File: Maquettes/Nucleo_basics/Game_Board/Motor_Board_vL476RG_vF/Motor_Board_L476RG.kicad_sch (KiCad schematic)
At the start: 41 parts, among them CON1 MikroE-Accelero, CON2 MikroE-nRF-S-module, J1 Speed_R, J10 Morpho_Gauche, J11 Morpho_Droite, J12 LED_1, J13 LED_2, J14 LED_3, J15 LED_4, J17 I2C_Visu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

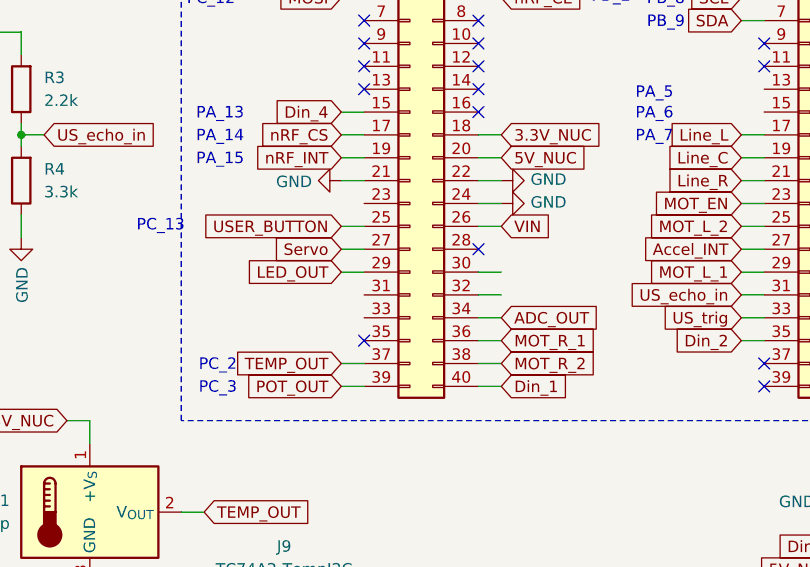
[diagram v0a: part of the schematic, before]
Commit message: Update Nucleo Basics / Remote and Robot Boards
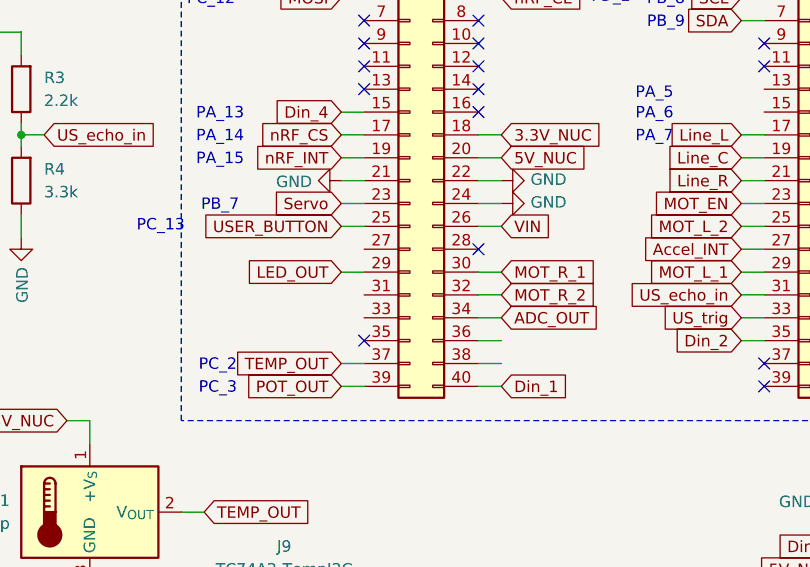
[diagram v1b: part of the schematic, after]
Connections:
- net MOT_R_1: now also J10.30 (Pin_30); no longer J10.36 (Pin_36)
- net MOT_R_2: now also J10.32 (Pin_32); no longer J10.38 (Pin_38)
- net Servo: now also J10.23 (Pin_23); no longer J10.27 (Pin_27)
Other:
- note added: "PB_7"
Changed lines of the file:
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@@
+	(wire
+		(pts
+			(xy 96.52 81.28) (xy 99.06 81.28)
+		)
+		(stroke
+			(width 0)
+			(type default)
+		)
+	)
 	(wire
 		(pts
@@
 	(wire
 		(pts
-			(xy 96.52 86.36) (xy 99.06 86.36)
-		)
-		(stroke
-			(width 0)
-			(type default)
-		)
-	)
-	(wire
-		(pts
 			(xy 199.39 154.94) (xy 196.85 154.94)
 		)
@@
 		)
 	)
+	(text "PB_7"
+		(exclude_from_sim no)
+		(at 83.058 81.534 0)
+		(effects
+			(font
+				(size 1.27 1.27)
+			)
+		)
+	)
 	(text "Nucleo BOARD"
 		(exclude_from_sim no)
@@
 	(global_label "Servo"
 		(shape input)
-		(at 96.52 86.36 180)
-		(effects
-			(font
-				(size 1.27 1.27)
-			)
-			(justify right)
-		)
-		(property "Intersheetrefs" "${INTERSHEET_REFS}"
-			(at 96.52 86.36 0)
+		(at 96.52 81.28 180)
+		(effects
+			(font
+				(size 1.27 1.27)
+			)
+			(justify right)
+		)
+		(property "Intersheetrefs" "${INTERSHEET_REFS}"
+			(at 96.52 81.28 0)
 			(effects
 				(font
@@
 	(global_label "MOT_R_2"
 		(shape input)
-		(at 114.3 99.06 0)
-		(effects
-			(font
-				(size 1.27 1.27)
-			)
-			(justify left)
-		)
-		(property "Intersheetrefs" "${INTERSHEET_REFS}"
-			(at 114.3 99.06 0)
+		(at 114.3 91.44 0)
+		(effects
+			(font
+				(size 1.27 1.27)
+			)
+			(justify left)
+		)
+		(property "Intersheetrefs" "${INTERSHEET_REFS}"
+			(at 114.3 91.44 0)
 			(effects
 				(font
@@
 	(global_label "MOT_R_1"
 		(shape input)
-		(at 114.3 96.52 0)
-		(effects
-			(font
-				(size 1.27 1.27)
-			)
-			(justify left)
-		)
-		(property "Intersheetrefs" "${INTERSHEET_REFS}"
-			(at 114.3 96.52 0)
-			(effects
-				(font
+		(at 114.3 88.9 0)
+		(effects
+			(font
+				(size 1.27 1.27)
+			)
+			(justify left)
+		)
+		(property "Intersheetrefs" "${INTERSHEET_REFS}"
+			(at 114.3 88.9 0)
+			(effects
+				(font

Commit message: Update Motor Board
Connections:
- net Line_R: now also J11.13 (Pin_13); no longer J11.21 (Pin_21)
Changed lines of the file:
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@@
+	(wire
+		(pts
+			(xy 140.97 68.58) (xy 143.51 68.58)
+		)
+		(stroke
+			(width 0)
+			(type default)
+		)
+	)
 	(wire
 		(pts
@@
 	(global_label "Line_R"
 		(shape input)
-		(at 140.97 78.74 180)
-		(effects
-			(font
-				(size 1.27 1.27)
-			)
-			(justify right)
-		)
-		(property "Intersheetrefs" "${INTERSHEET_REFS}"
-			(at 140.97 78.74 0)
-			(effects
-				(font
+		(at 140.97 68.58 180)
+		(effects
+			(font
+				(size 1.27 1.27)
+			)
+			(justify right)
+		)
+		(property "Intersheetrefs" "${INTERSHEET_REFS}"
+			(at 140.97 68.58 0)
+			(effects
+				(font

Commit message: Update Robot Board
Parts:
- J12, J13, J14, J15: footprint Connector_PinSocket_2.54mm:PinSocket_1x04_P2.54mm_Vertical -> Connector_PinSocket_2.54mm:PinSocket_1x04_P2.54mm_Horizontal
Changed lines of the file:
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@@
 			)
 		)
-		(property "Footprint" "Connector_PinSocket_2.54mm:PinSocket_1x04_P2.54mm_Vertical"
+		(property "Footprint" "Connector_PinSocket_2.54mm:PinSocket_1x04_P2.54mm_Horizontal"
 			(at 160.02 142.24 0)
 			(effects
@@
 			)
 		)
-		(property "Footprint" "Connector_PinSocket_2.54mm:PinSocket_1x04_P2.54mm_Vertical"
+		(property "Footprint" "Connector_PinSocket_2.54mm:PinSocket_1x04_P2.54mm_Horizontal"
 			(at 160.02 116.84 0)
 			(effects
@@
 			)
 		)
-		(property "Footprint" "Connector_PinSocket_2.54mm:PinSocket_1x04_P2.54mm_Vertical"
+		(property "Footprint" "Connector_PinSocket_2.54mm:PinSocket_1x04_P2.54mm_Horizontal"
 			(at 160.02 129.54 0)
 			(effects
@@
 			)
 		)
-		(property "Footprint" "Connector_PinSocket_2.54mm:PinSocket_1x04_P2.54mm_Vertical"
+		(property "Footprint" "Connector_PinSocket_2.54mm:PinSocket_1x04_P2.54mm_Horizontal"
 			(at 160.02 154.94 0)
 			(effects

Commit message: Update Boards
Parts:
- added D2: LED, LED_THT:LED_D3.0mm_Clear, symbol Device:LED
- added R8: 100, Resistor_THT:R_Axial_DIN0207_L6.3mm_D2.5mm_P10.16mm_Horizontal, symbol Device:R
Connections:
- net GND: now also D2.1 (K)
- net LED_OUT2: now reaches J11.32 (Pin_32), J23.6 (Pin_6)
- net LED_OUT2: now also R8.2
- new net: D2.2 (A), R8.1

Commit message: Update Robot and Remote Boards
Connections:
- net 3.3V_NUC: no longer J6.4 (Pin_4)
- net 5V: now also J6.4 (Pin_4)
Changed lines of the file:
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@@
+		)
+	)
+	(global_label "5V"
+		(shape input)
+		(at 57.15 45.72 0)
+		(effects
+			(font
+				(size 1.27 1.27)
+			)
+			(justify left)
+		)
+		(property "Intersheetrefs" "${INTERSHEET_REFS}"
+			(at 57.15 45.72 0)
+			(effects
+				(font
+					(size 1.27 1.27)
+				)
+				(hide yes)
+			)
 		)
 	)
@@
 			(effects
 				(font
-					(size 1.27 1.27)
-				)
-				(hide yes)
-			)
-		)
-	)
-	(global_label "3.3V_NUC"
-		(shape input)
-		(at 57.15 45.72 0)
-		(effects
-			(font
-				(size 1.27 1.27)
-			)
-			(justify left)
-		)
-		(property "Intersheetrefs" "${INTERSHEET_REFS}"
-			(at 57.15 45.72 0)
-			(effects
-				(font

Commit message: Update Robot board for Joy It Car
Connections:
- net LED_OUT: now also J11.21 (Pin_21); no longer J10.29 (Pin_29)
- no-connect marks 29 -> 33
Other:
- note added: "PC_7"
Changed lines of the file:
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@@
 	)
 	(no_connect
+		(at 99.06 93.98)
+	)
+	(no_connect
 		(at 154.94 142.24)
 	)
 	(no_connect
+		(at 99.06 88.9)
+	)
+	(no_connect
 		(at 111.76 68.58)
 	)
@@
 	)
 	(no_connect
+		(at 99.06 86.36)
+	)
+	(no_connect
 		(at 156.21 99.06)
 	)
@@
 	)
 	(no_connect
+		(at 99.06 91.44)
+	)
+	(no_connect
 		(at 143.51 53.34)
 	)
@@
 	(wire
 		(pts
-			(xy 96.52 88.9) (xy 99.06 88.9)
-		)
-		(stroke
-			(width 0)
-			(type default)
-		)
-	)
-	(wire
-		(pts
 			(xy 156.21 88.9) (xy 158.75 88.9)
 		)
@@
 		)
 	)
+	(text "PC_7"
+		(exclude_from_sim no)
+		(at 127.254 78.994 0)
+		(effects
+			(font
+				(size 1.27 1.27)
+			)
+		)
+	)
 	(text "PB_9"
 		(exclude_from_sim no)
@@
 	(text "PC_4"
 		(exclude_from_sim no)
-		(at 168.656 96.774 0)
+		(at 177.038 97.028 0)
 		(effects
 			(font
@@
 	(global_label "LED_OUT"
 		(shape input)
-		(at 96.52 88.9 180)
+		(at 140.97 78.74 180)
 		(effects
 			(font
@@
 		)
 		(property "Intersheetrefs" "${INTERSHEET_REFS}"
-			(at 96.52 88.9 0)
+			(at 140.97 78.74 0)
 			(effects
 				(font

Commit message: Update Robot Board
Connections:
- net GND: now also CON1.P3 (CS), CON1.P5 (MISO)
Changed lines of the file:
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@@
 	(wire
 		(pts
+			(xy 69.85 163.83) (xy 72.39 163.83)
+		)
+		(stroke
+			(width 0)
+			(type default)
+		)
+	)
+	(wire
+		(pts
 			(xy 203.2 38.1) (xy 205.74 38.1)
 		)
@@
 		)
 	)
+	(label "SA1"
+		(at 71.12 163.83 0)
+		(fields_autoplaced yes)
+		(effects
+			(font
+				(size 1.27 1.27)
+			)
+			(justify left bottom)
+		)
+	)
 	(global_label "US_echo"
 		(shape input)
@@
 	)
 	(symbol
+		(lib_id "power:GND")
+		(at 69.85 163.83 270)
+		(unit 1)
+		(exclude_from_sim no)
+		(in_bom yes)
+		(on_board yes)
+		(dnp no)
+		(property "Reference" "#PWR036"
+			(at 63.5 163.83 0)
+			(effects
+				(font
+					(size 1.27 1.27)
+				)
+				(hide yes)
+			)
+		)
+		(property "Value" "GND"
+			(at 66.5988 163.957 90)
+			(effects
+				(font
+					(size 1.27 1.27)
+				)
+				(justify right)
+			)
+		)
+		(property "Footprint" ""
+			(at 69.85 163.83 0)
+			(effects
+				(font
+					(size 1.27 1.27)
+				)
+				(hide yes)
+			)
+		)
+		(property "Datasheet" ""
+			(at 69.85 163.83 0)
+			(effects
+				(font
+					(size 1.27 1.27)
+				)
+				(hide yes)
+			)
+		)
+		(property "Description" ""
+			(at 69.85 163.83 0)
+			(effects
+				(font
+					(size 1.27 1.27)
+				)
+				(hide yes)
+			)
+		)
+		(pin "1"
+		)
+		(instances
+			(project "Motor_Board_L476RG"
+				(path "/44ad8000-4ee7-4966-8fe6-195894dfb602"
+					(reference "#PWR036")
+					(unit 1)
+				)
+			)
+		)
+	)
+	(symbol
 		(lib_id "mikroBUS:MIKROBUS_MODULE_CONN")
 		(at 238.76 163.83 0)
@@
 					(unit 1)
 				)
+			)
+		)
+	)
+	(symbol
+		(lib_id "power:GND")
+		(at 69.85 173.99 270)
+		(unit 1)
+		(exclude_from_sim no)
+		(in_bom yes)
+		(on_board yes)
+		(dnp no)
+		(property "Reference" "#PWR035"
+			(at 63.5 173.99 0)
+			(effects
+				(font
+					(size 1.27 1.27)
+				)
+				(hide yes)
+			)
+		)
+		(property "Value" "GND"
+			(at 66.5988 174.117 90)
+			(effects
+				(font
+					(size 1.27 1.27)
+				)
+				(justify right)
+			)
+		)
+		(property "Footprint" ""
+			(at 69.85 173.99 0)
+			(effects
+				(font
+					(size 1.27 1.27)
+				)
+				(hide yes)
+			)
+		)
+		(property "Datasheet" ""
+			(at 69.85 173.99 0)
+			(effects
+				(font
+					(size 1.27 1.27)
+				)
+				(hide yes)
+			)
+		)
+		(property "Description" ""
+			(at 69.85 173.99 0)
+			(effects
+				(font
+					(size 1.27 1.27)
+				)
+				(hide yes)
+			)
+		)
+		(pin "1"
+		)
+		(instances
+			(project "Motor_Board_L476RG"
+				(path "/44ad8000-4ee7-4966-8fe6-195894dfb602"
+					(reference "#PWR035")
+					(unit 1)
+				)

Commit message: Update Robot Board
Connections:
- net US_echo_in: now also J11.33 (Pin_33); no longer J11.31 (Pin_31)
- net US_trig: now also J11.31 (Pin_31); no longer J11.33 (Pin_33)
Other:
- note added: "PB_3"
- note added: "PB_5"
- moved on the sheet: J11, J17, J18, J19, J20, J23, R6, R7
